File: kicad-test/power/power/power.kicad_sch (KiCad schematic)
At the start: 77 parts, among them J1 GND, J10 Conn_01x04_Pin, J2 GND2, J3 +15V, J4 -15V, J5 +5V, J6 +48V, J7 USB_C_Receptacle_USB2.0_16P, J8 PH_EN, J9 USB_C_Receptacle_USB2.0_16P, T1 475uH, U18 PTN5150AHXMP, U20 TPS7A39, U21 SN6505BDBV, U22 TPS2116DRL, U23 TPS62172DSG, U25 TPS7A2009, U26 TPS62171DSG, U27 TPS7A4101, U28 TPS61391, U30 CH224K

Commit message: added test points
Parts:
- added J11: EN_15V, Connector_PinHeader_2.54mm:PinHeader_1x02_P2.54mm_Vertical, symbol Connector:Conn_01x02_Pin
- added J12: EN_3V3, Connector_PinHeader_2.54mm:PinHeader_1x02_P2.54mm_Vertical, symbol Connector:Conn_01x02_Pin
- added J13: EN_1V8_0V9, Connector_PinHeader_2.54mm:PinHeader_1x02_P2.54mm_Vertical, symbol Connector:Conn_01x02_Pin
- added J14: EN_PH_SRC, Connector_PinHeader_2.54mm:PinHeader_1x02_P2.54mm_Vertical, symbol Connector:Conn_01x02_Pin
- added TP1: PH_MID, TestPoint:TestPoint_Keystone_5010-5014_Multipurpose, symbol Connector:TestPoint
- added TP2: 15V_MID, TestPoint:TestPoint_Keystone_5010-5014_Multipurpose, symbol Connector:TestPoint
- added TP3: 5V_EXT, TestPoint:TestPoint_Keystone_5010-5014_Multipurpose, symbol Connector:TestPoint
- added TP4: 5V_PD, TestPoint:TestPoint_Keystone_5010-5014_Multipurpose, symbol Connector:TestPoint
- added TP5: 5V_MID, TestPoint:TestPoint_Keystone_5010-5014_Multipurpose, symbol Connector:TestPoint
- J8: value PH_EN -> EN_PH
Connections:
- net +5V: now also J11.2 (Pin_2), J12.2 (Pin_2), J13.2 (Pin_2), J14.2 (Pin_2), TP5.1; no longer C161.1, C165.1, C167.1, C171.1, L3.1, R108.2, T1.2, U21.2 (VCC), U23.2 (VIN), U23.3 (EN), U26.2 (VIN), U26.3 (EN), U28.10 (VIN)
- net +5V_EXT: now also TP3.1
- net VBUS: now also TP4.1
- net at C172.1, C173.1, C174.1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: now also TP1.1
- net at C158.1, D64.1 (K), R105.1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: now also TP2.1
- new net: C161.1, J11.1 (Pin_1), R108.2, T1.2, U21.2 (VCC)
- new net: C171.1, J14.1 (Pin_1), L3.1, U28.10 (VIN)
- new net: C167.1, J13.1 (Pin_1), U26.2 (VIN), U26.3 (EN)
- new net: C165.1, J12.1 (Pin_1), U23.2 (VIN), U23.3 (EN)
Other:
- note removed: "ref: 2."
- note removed: "ref: 4."

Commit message: board footprint layout
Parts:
- removed J14: EN_PH_SRC, Connector_PinHeader_2.54mm:PinHeader_1x02_P2.54mm_Vertical, symbol Connector:Conn_01x02_Pin
- removed U25: TPS7A2009, Package_SON:Texas_X2SON-4_1x1mm_P0.65mm, symbol Regulator_Linear:TPS7A20xxxDQN
- added C199, C200: 1uF, Capacitor_SMD:C_0805_2012Metric_Pad1.18x1.45mm_HandSolder, symbol Device:C_Small
- added J15: EN_0V9, Connector_PinHeader_2.54mm:PinHeader_1x02_P2.54mm_Vertical, symbol Connector:Conn_01x02_Pin
- added R124, R125, R126: 100k, Resistor_SMD:R_0805_2012Metric_Pad1.20x1.40mm_HandSolder, symbol Device:R_US
- added U1: TPS7A2009, Package_TO_SOT_SMD:SOT-23-5, symbol Regulator_Linear:TPS7A20xxxDBV
- R121: value 10k -> 100k
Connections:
- net +0V9: now also U1.5 (OUT)
- net +1V8: now also J15.2 (Pin_2), U1.1 (IN)
- net +3V3: now also J8.2 (Pin_2); no longer J8.1 (Pin_1)
- net +5V: now also C161.1, C165.1, C167.1, C171.1, L3.1, R108.2, T1.2, U21.2 (VCC), U23.2 (VIN), U26.2 (VIN), U28.10 (VIN); no longer J11.2 (Pin_2)
- net +5V_EXT: now also C199.1
- net Earth: now also C199.2, C200.1, R124.2, R125.2, R126.2, U1.2 (GND)
- net VBUS: now also C200.2
- net at J13.1 (Pin_1), U26.3 (EN): now also R124.1; no longer C167.1, U26.2 (VIN)
- net at U21.5 (EN): now also J11.1 (Pin_1); no longer R108.1
- net at J12.1 (Pin_1), U23.3 (EN): now also R125.1; no longer C165.1, U23.2 (VIN)
- net at R121.1, U28.13 (EN): now also J8.1 (Pin_1); no longer J8.2 (Pin_2)
- new net: J11.2 (Pin_2), R108.1
- new net: J15.1 (Pin_1), R126.1, U1.3 (EN)
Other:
- moved on the sheet: C165, C166, C169, J11, J12, J13, L1, R112, U23

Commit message: power board first draft
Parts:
- R116, R117, R122, R94: footprint Resistor_SMD:R_0603_1608Metric_Pad0.98x0.95mm_HandSolder -> Resistor_SMD:R_0805_2012Metric_Pad1.20x1.40mm_HandSolder
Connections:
- net CC1: no longer J7.A5 (CC1), U18.1 (CC1)
- net CC2: no longer J7.B5 (CC2), U18.2 (CC2)
- new net CC1_EXT: J7.A5 (CC1), U18.1 (CC1)
- new net CC2_EXT: J7.B5 (CC2), U18.2 (CC2)
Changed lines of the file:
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@@
 	(wire
 		(pts
-			(xy 264.16 78.74) (xy 264.16 80.01)
-		)
-		(stroke
-			(width 0)
-			(type default)
-		)
-	)
-	(wire
-		(pts
 			(xy 83.82 247.65) (xy 83.82 252.73)
 		)
@@
 		)
 	)
-	(label "CC2"
+	(label "CC2_EXT"
 		(at 347.98 176.53 180)
 		(effects
@@
 		)
 	)
-	(label "CC1"
+	(label "CC1_EXT"
 		(at 347.98 173.99 180)
 		(effects
@@
 		)
 	)
-	(label "CC2"
+	(label "CC2_EXT"
 		(at 379.73 133.35 0)
 		(effects
@@
 		)
 	)
-	(label "CC1"
+	(label "CC1_EXT"
 		(at 379.73 130.81 0)
 		(effects
@@
 			)
 		)
-		(property "Footprint" "Resistor_SMD:R_0603_1608Metric_Pad0.98x0.95mm_HandSolder"
+		(property "Footprint" "Resistor_SMD:R_0805_2012Metric_Pad1.20x1.40mm_HandSolder"
 			(at 318.77 123.19 0)
 			(hide yes)
@@
 			)
 		)
-		(property "Footprint" "Resistor_SMD:R_0603_1608Metric_Pad0.98x0.95mm_HandSolder"
+		(property "Footprint" "Resistor_SMD:R_0805_2012Metric_Pad1.20x1.40mm_HandSolder"
 			(at 252.73 62.23 0)
 			(hide yes)
@@
 			)
 		)
-		(property "Footprint" "Resistor_SMD:R_0603_1608Metric_Pad0.98x0.95mm_HandSolder"
+		(property "Footprint" "Resistor_SMD:R_0805_2012Metric_Pad1.20x1.40mm_HandSolder"
 			(at 264.16 68.58 0)
 			(hide yes)
@@
 			)
 		)
-		(property "Footprint" "Resistor_SMD:R_0603_1608Metric_Pad0.98x0.95mm_HandSolder"
+		(property "Footprint" "Resistor_SMD:R_0805_2012Metric_Pad1.20x1.40mm_HandSolder"
 			(at 330.2 129.54 0)
 			(hide yes)

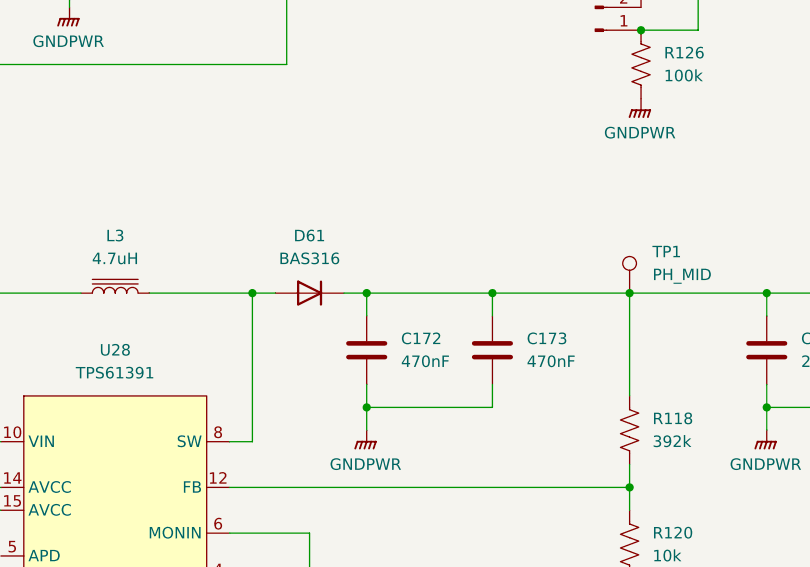
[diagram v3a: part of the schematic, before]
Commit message: trace widths
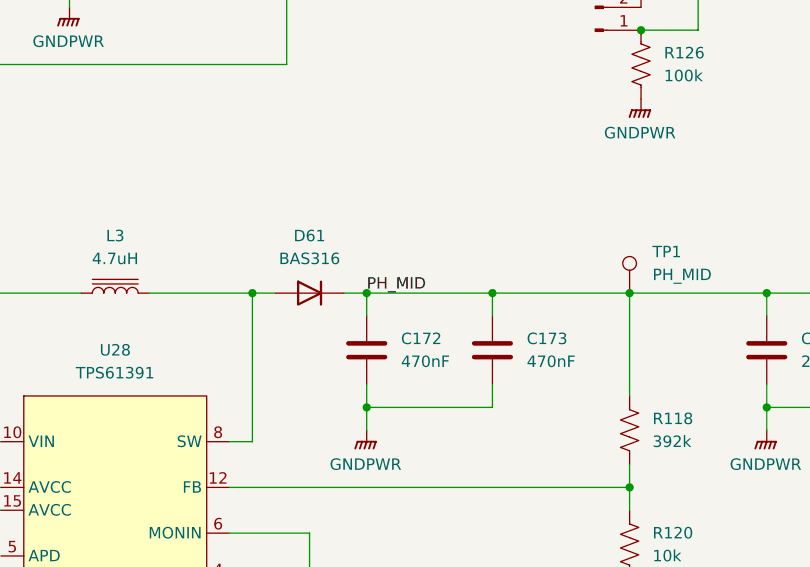
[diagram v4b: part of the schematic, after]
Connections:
- net PH_MID: now reaches C172.1, C173.1, C174.1, C175.1, D61.1 (K), R118.1, TP1.1, U27.5 (EN), U27.8 (IN)
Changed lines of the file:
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@@
+		)
+	)
+	(label "PH_MID"
+		(at 90.17 195.58 0)
+		(effects
+			(font
+				(size 1.27 1.27)
+			)
+			(justify left bottom)
 		)
 	)

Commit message: bom update
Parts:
- C1: renamed from C161; LCSC (none) -> C15850
- C10: renamed from C162; LCSC (none) -> C15850
- C11: renamed from C169; LCSC (none) -> C28323
- C12: renamed from C159; LCSC (none) -> C15850
- C13: renamed from C174; LCSC (none) -> C377773
- C14: renamed from C170; LCSC (none) -> C28323
- C15: renamed from C175; LCSC (none) -> C377773
- C16: renamed from C160; LCSC (none) -> C15850
- C17: renamed from C176; LCSC (none) -> C1710
- C18: renamed from C157; LCSC (none) -> C15850
- C19: renamed from C164; LCSC (none) -> C15850
- C2: renamed from C165; LCSC (none) -> C15850
- C20: renamed from C177; LCSC (none) -> C15850
- C21: renamed from C178; LCSC (none) -> C15850
- C22: renamed from C181; LCSC (none) -> C28323
- C23: renamed from C150; LCSC (none) -> C49678
- C24: renamed from C197; LCSC (none) -> C49678
- C25: renamed from C151; LCSC (none) -> C15850
- C26: renamed from C198; LCSC (none) -> C15850
- C27: renamed from C200; LCSC (none) -> C28323
- C28: renamed from C199; LCSC (none) -> C28323
- C29: renamed from C163; LCSC (none) -> C45783
- C3: renamed from C167; LCSC (none) -> C15850
- C4: renamed from C171; LCSC (none) -> C1779
- C5: renamed from C172; LCSC (none) -> C13967
- C6: renamed from C166; LCSC (none) -> C45783
- C7: renamed from C168; LCSC (none) -> C45783
- C8: renamed from C173; LCSC (none) -> C13967
- C9: renamed from C158; LCSC (none) -> C15850
- D1: renamed from D61; LCSC (none) -> C8488
- D2: renamed from D64; LCSC (none) -> C77339
- D3: renamed from D69; LCSC (none) -> C77339
- D4: renamed from D2; footprint LED_THT:LED_D5.0mm -> LED_SMD:LED_0805_2012Metric_Pad1.15x1.40mm_HandSolder; LCSC (none) -> C84256
- D5: renamed from D1; footprint LED_THT:LED_D5.0mm -> LED_SMD:LED_0805_2012Metric_Pad1.15x1.40mm_HandSolder; LCSC (none) -> C84256
- J13: renamed from J9; LCSC (none) -> C165948
- J14: renamed from J7; LCSC (none) -> C165948
- L1: renamed from L3; LCSC (none) -> C3223763
- L2: renamed from L1; footprint Inductor_SMD:L_Wuerth_PMCI-201610 -> Inductor_SMD_Wurth:L_Wurth_WE-LQSH-3012; LCSC (none) -> C6364793
- L3: renamed from L2; footprint Inductor_SMD:L_Wuerth_PMCI-201610 -> Inductor_SMD_Wurth:L_Wurth_WE-LQSH-3012; LCSC (none) -> C6364793
- R1: renamed from R125; LCSC (none) -> C149504
- R11: renamed from R107; LCSC (none) -> C149504
- R12: renamed from R106; LCSC (none) -> C17414
- R15: renamed from R104; LCSC (none) -> C17414
- R17: renamed from R119; LCSC (none) -> C17444
- R18: renamed from R117; LCSC (none) -> C17513
- R19: renamed from R116; LCSC (none) -> C17414
- R2: renamed from R124; LCSC (none) -> C149504
- R20: renamed from R123; LCSC (none) -> C17414
- R21: renamed from R122; LCSC (none) -> C17513
- R23: renamed from R111; LCSC (none) -> C149504
- R24: renamed from R94; LCSC (none) -> C17414
- R3: renamed from R121; LCSC (none) -> C149504
- R4: renamed from R108; LCSC (none) -> C17414
- R5: renamed from R112; LCSC (none) -> C149504
- R6: renamed from R114; LCSC (none) -> C149504
- R8: renamed from R120; LCSC (none) -> C17414
- R9: renamed from R126; LCSC (none) -> C149504
- T1: LCSC (none) -> C249186
- U1: renamed from U23; LCSC (none) -> C59873
- U10: renamed from U22; LCSC (none) -> C3235557
- U2: renamed from U26; LCSC (none) -> C2071102
- U3: renamed from U21; LCSC (none) -> C74518
- U4: renamed from U28; LCSC (none) -> C1852151
- U5: renamed from U1; LCSC (none) -> C2861215
- U6: renamed from U20; LCSC (none) -> C2685819
- U7: renamed from U27; LCSC (none) -> C111739
- U8: renamed from U30; LCSC (none) -> C970725
- U9: renamed from U18; LCSC (none) -> C2651889
- renumbered J12 to J1, J1 to J10, J10 to J11, J2 to J12, J13 to J2, J8 to J3, J11 to J4, J15 to J5, J3 to J6, J4 to J7, J5 to J8, J6 to J9, R105 to R10, R103 to R13, R109 to R14, R115 to R16, R110 to R22, R118 to R7, TP4 to TP3, TP3 to TP4

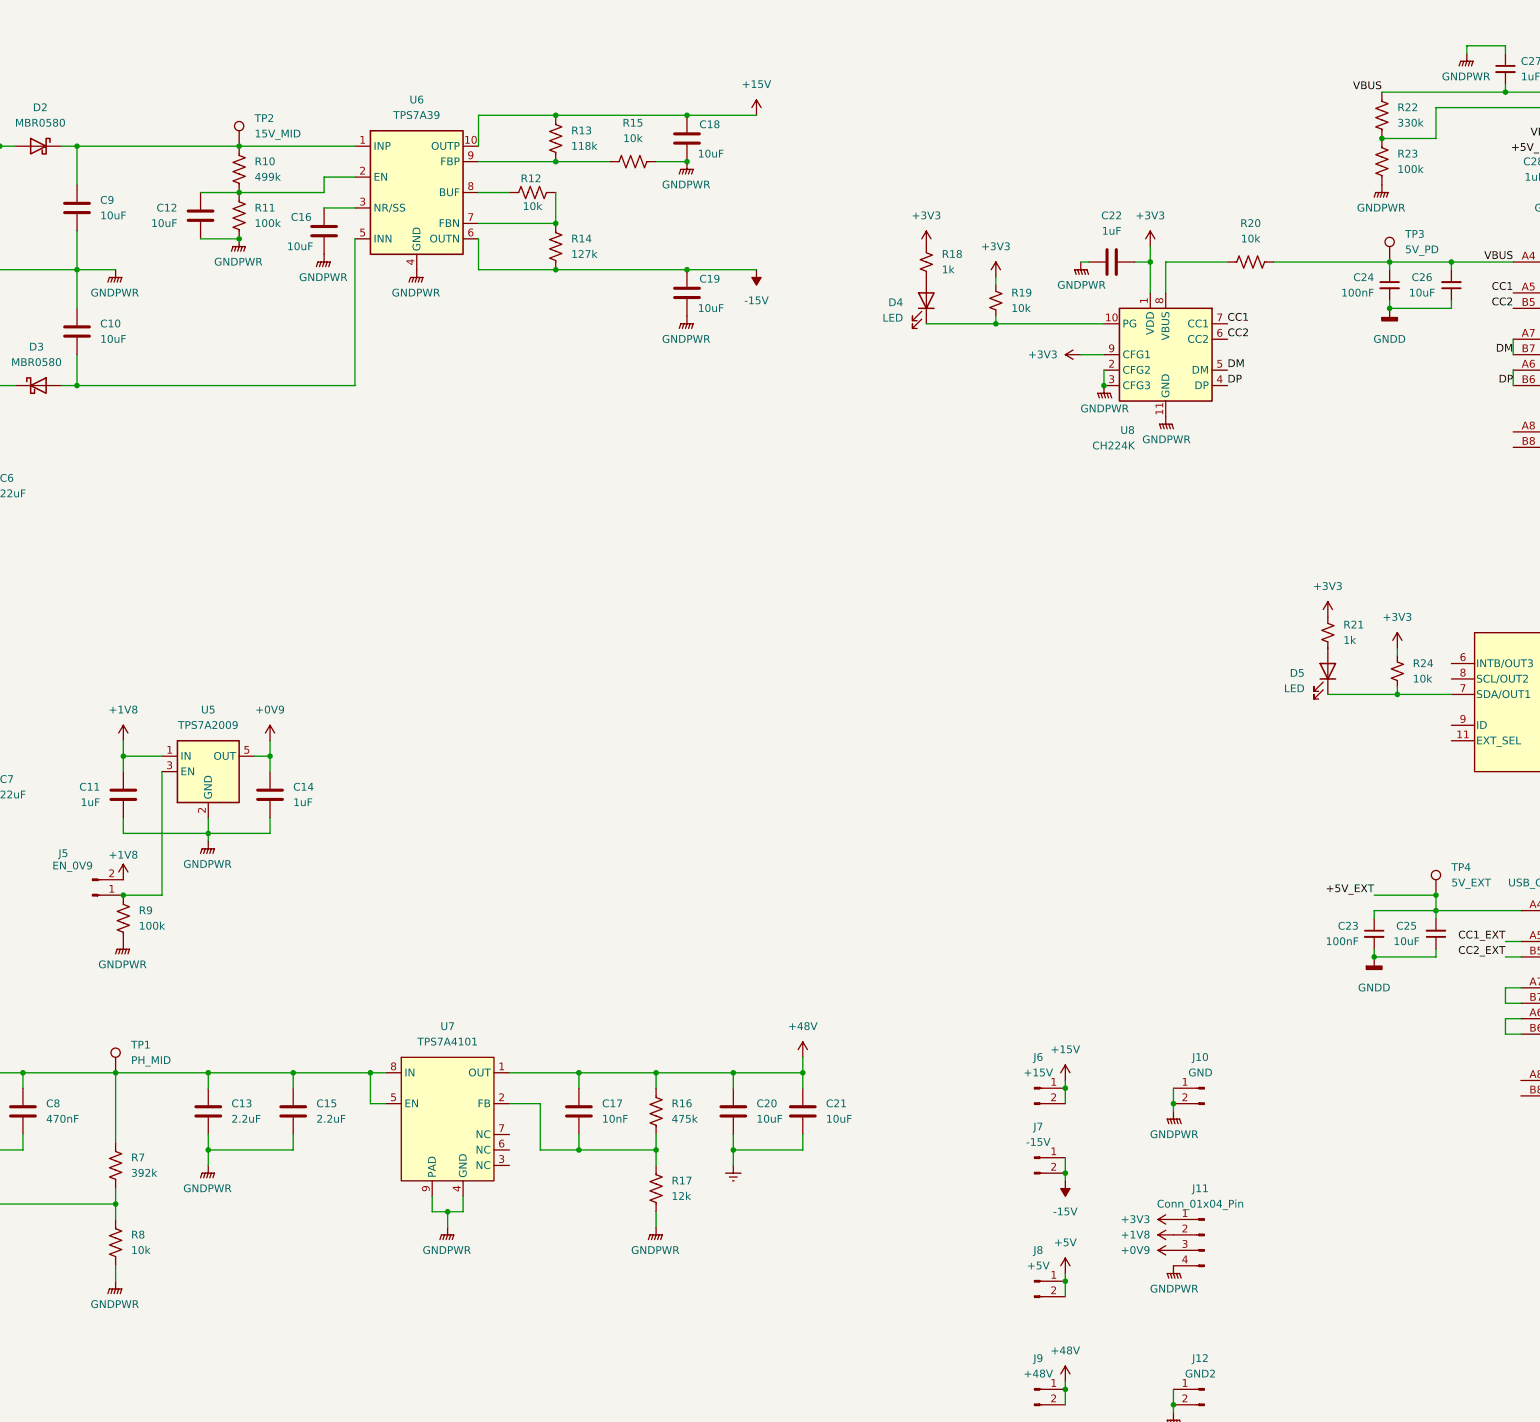
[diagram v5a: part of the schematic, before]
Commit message: standard jlc resistor values
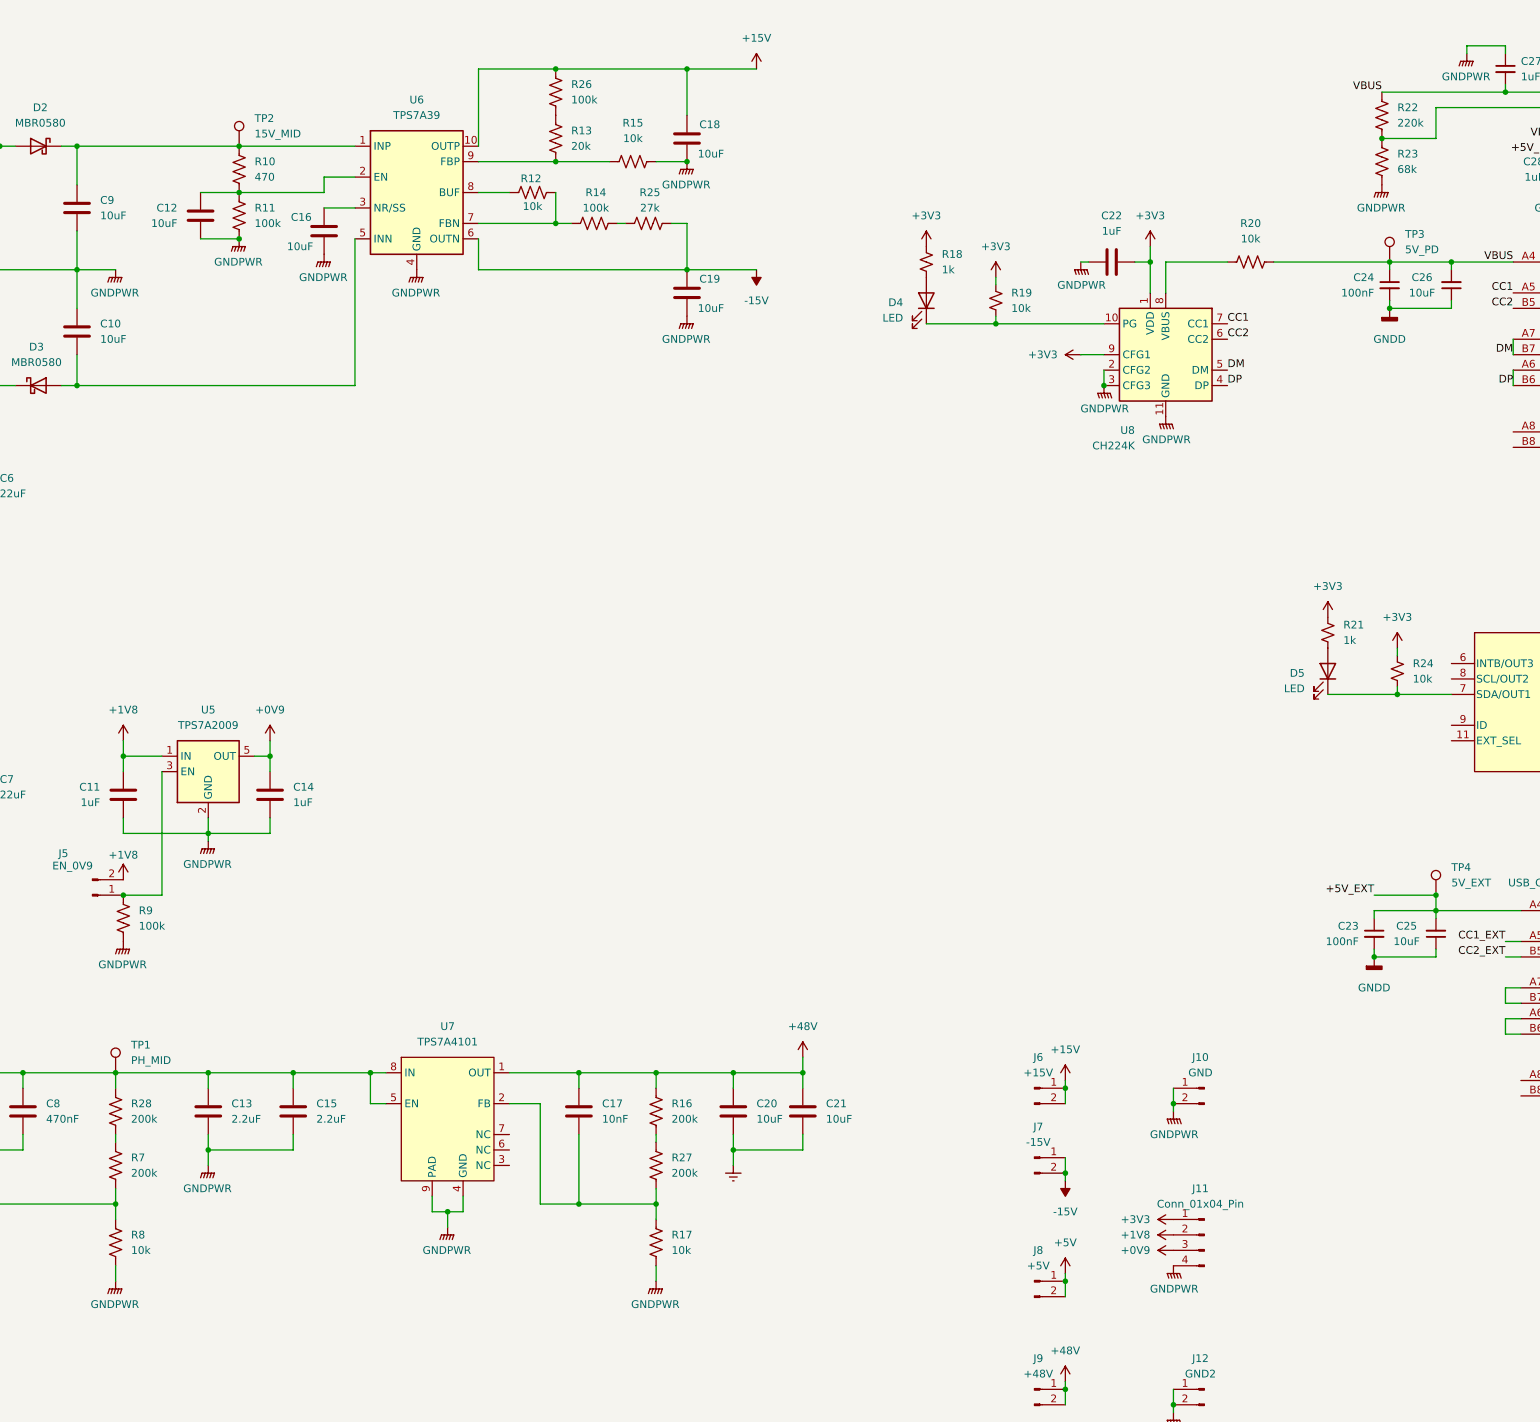
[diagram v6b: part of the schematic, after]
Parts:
- added R25: 27k, Resistor_SMD:R_0805_2012Metric_Pad1.20x1.40mm_HandSolder, symbol Device:R_US
- added R26: 100k, Resistor_SMD:R_0805_2012Metric_Pad1.20x1.40mm_HandSolder, symbol Device:R_US
- added R27, R28: 200k, Resistor_SMD:R_0805_2012Metric_Pad1.20x1.40mm_HandSolder, symbol Device:R_US
- R1, R11, R2, R3, R5, R6, R9: LCSC C149504 -> (none)
- R10: value 499k -> 470
- R12, R15, R19, R20, R24, R4, R8: LCSC C17414 -> (none)
- R13: value 118k -> 20k
- R14: value 127k -> 100k
- R16: value 475k -> 200k
- R17: value 12k -> 10k; LCSC C17444 -> (none)
- R18, R21: LCSC C17513 -> (none)
- R22: value 330k -> 220k
- R23: value 100k -> 68k; LCSC C149504 -> (none)
- R7: value 392k -> 200k
- T1: LCSC C249186 -> (none)
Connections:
- net +15V: now also R26.1; no longer R13.1
- net -15V: now also R25.2; no longer R14.2
- net PH_MID: now also R28.1; no longer R7.1
- net at C17.2, R17.1, U7.2 (FB): now also R27.2; no longer R16.2
- new net: R28.2, R7.1
- new net: R16.2, R27.1
- new net: R14.2, R25.1
- new net: R13.1, R26.2
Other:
- moved on the sheet: R14, R17

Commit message: add JLC and MPN to BOM
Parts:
- C1, C10, C12, C16, C18, C19, C2, C20, C21, C25, C26, C3, C9: MPN (none) -> CL21A106KAYNNNE
- C11, C14, C22, C27, C28: MPN (none) -> CL21B105KBFNNNE
- C13, C15: MPN (none) -> CL21A225KBQNNNE
- C17: MPN (none) -> CL21B103KBANNNC
- C23, C24: MPN (none) -> CC0805KRX7R9BB104
- C29, C6, C7: MPN (none) -> CL21A226MAQNNNE
- C4: MPN (none) -> CL21A475KAQNNNE
- C5, C8: MPN (none) -> CL21B474KBFNNNE
- D1: MPN (none) -> BAS316
- D2, D3: MPN (none) -> MBR0580
- D4, D5: MPN (none) -> NCD0805R1
- J13, J14: MPN (none) -> TYPE-C-31-M-12
- L1: MPN (none) -> DFE201612E-4R7M=P2
- L2, L3: MPN (none) -> ANR3015T2R2M
- R1, R11, R14, R2, R26, R3, R5, R6, R9: LCSC (none) -> C149504; MPN (none) -> 0805W8F1003T5E
- R10: LCSC (none) -> C17710; MPN (none) -> 0805W8F4700T5E
- R12, R15, R17, R19, R20, R24, R4, R8: LCSC (none) -> C17414; MPN (none) -> 0805W8F1002T5E
- R13: LCSC (none) -> C4328; MPN (none) -> 0805W8F2002T5E
- R16, R27, R28, R7: LCSC (none) -> C17539; MPN (none) -> 0805W8F2003T5E
- R18, R21: LCSC (none) -> C17513; MPN (none) -> 0805W8F1001T5E
- R22: LCSC (none) -> C17556; MPN (none) -> 0805W8F2203T5E
- R23: LCSC (none) -> C17801; MPN (none) -> 0805W8F6802T5E
- R25: LCSC (none) -> C17593; MPN (none) -> 0805W8F2702T5E
- T1: LCSC (none) -> C249186; MPN (none) -> 760390015
- U1: MPN (none) -> TPS62172DSGR
- U10: MPN (none) -> TPS2116DRLR
- U2: MPN (none) -> TPS62171DSGR
- U3: MPN (none) -> SN6505BDBVR
- U4: MPN (none) -> TPS61391RTER
- U5: MPN (none) -> TPS7A2009PDBVR
- U6: MPN (none) -> TPS7A3901DSCR
- U7: MPN (none) -> TPS7A4101DGNR
- U8: MPN (none) -> CH224K
- U9: MPN (none) -> PTN5150AHXMP
